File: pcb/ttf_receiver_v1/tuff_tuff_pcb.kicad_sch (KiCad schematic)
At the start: 46 parts, among them J1 Conn_01x02_Socket, J2 Conn_ST_STDC14, J3 TC2070-IDC, J4 Conn_01x02_Pin, J5 Conn_01x04_Pin, Q1 DMG2301L, Q2 DMG3402L, Q3 DMG2301L, Q4 DMG3402L, Q5 DMG2301L, Q6 DMG3402L, Q7 DMG2301L, Q8 DMG3402L, U1 451-00001, U2 TLV76733QWDRBxQ1, U3 MT3608, Y1 Crystal

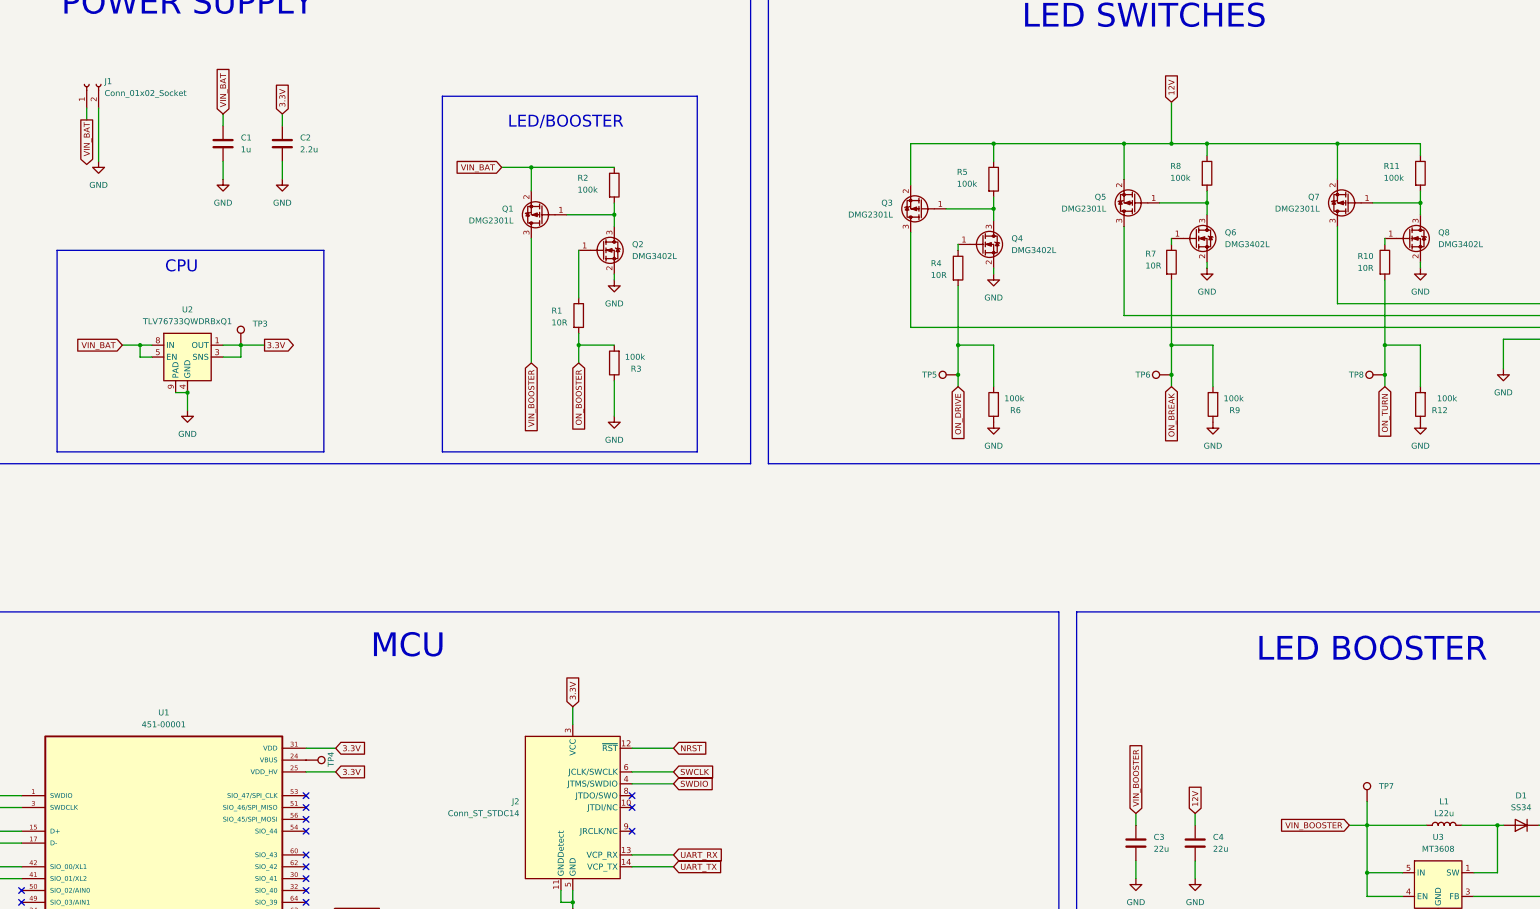
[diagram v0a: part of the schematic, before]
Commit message: feat: Updated ttl schematic
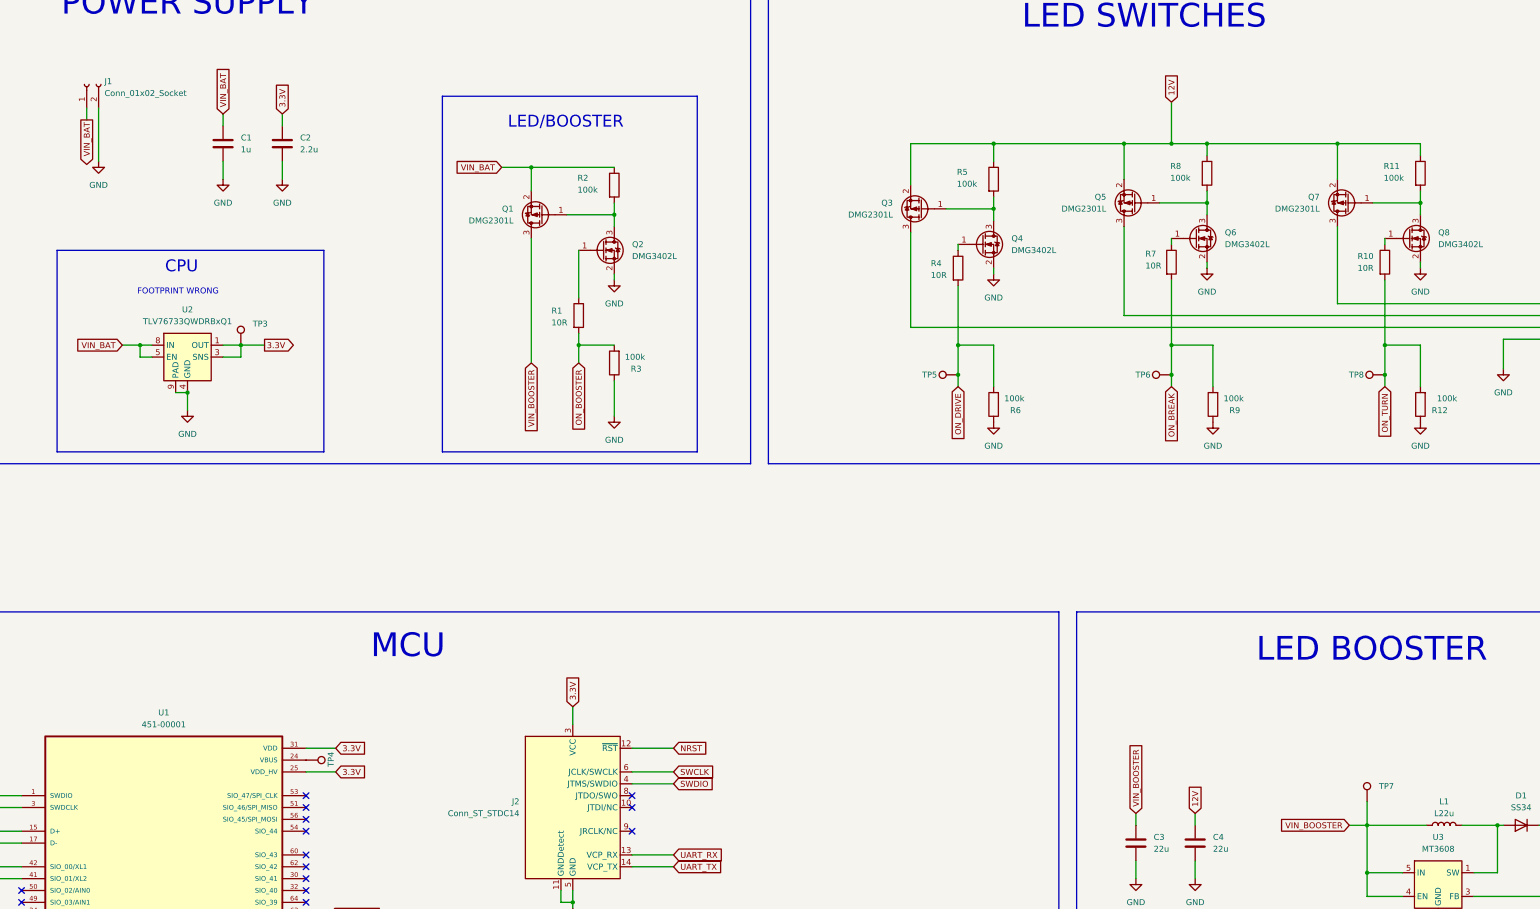
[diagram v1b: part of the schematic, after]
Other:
- note added: "FOOTPRINT WRONG"
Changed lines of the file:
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@@
 (kicad_sch
-	(version 20231120)
+	(version 20250114)
 	(generator "eeschema")
-	(generator_version "8.0")
+	(generator_version "9.0")
 	(paper "A3")
 	(title_block
 		(title "ttl_receiver")
 	)
+	(rectangle
+		(start 44.45 74.93)
+		(end 101.6 118.11)
+		(stroke
+			(width 0)
+			(type default)
+		)
+		(fill
+			(type none)
+		)
+	)
+	(rectangle
+		(start 20.32 16.51)
+		(end 193.04 120.65)
+		(stroke
+			(width 0)
+			(type default)
+		)
+		(fill
+			(type none)
+		)
+	)
+	(rectangle
+		(start 196.85 16.51)
+		(end 398.78 120.65)
+		(stroke
+			(width 0)
+			(type default)
+		)
+		(fill
+			(type none)
+		)
+	)
+	(rectangle
+		(start 127 41.91)
+		(end 181.61 118.11)
+		(stroke
+			(width 0)
+			(type default)
+		)
+		(fill
+			(type none)
+		)
+	)
+	(rectangle
+		(start 15.24 152.4)
+		(end 259.08 283.21)
+		(stroke
+			(width 0)
+			(type default)
+		)
+		(fill
+			(type none)
+		)
+	)
+	(rectangle
+		(start 262.89 152.4)
+		(end 400.05 247.65)
+		(stroke
+			(width 0)
+			(type default)
+		)
+		(fill
+			(type none)
+		)
+	)
+	(text "LED/BOOSTER"
+		(exclude_from_sim no)
+		(at 153.416 47.498 0)
+		(effects
+			(font
+				(size 2.54 2.54)
+			)
+		)
+	)
+	(text "LED BOOSTER"
+		(exclude_from_sim no)
+		(at 326.136 160.528 0)
+		(effects
+			(font
+				(size 5.08 5.08)
+			)
+		)
+	)
+	(text "FOOTPRINT WRONG"
+		(exclude_from_sim no)
+		(at 70.358 83.82 0)
+		(effects
+			(font
+				(size 1.27 1.27)
+			)
+		)
+	)
+	(text "MCU"
+		(exclude_from_sim no)
+		(at 119.634 159.766 0)
+		(effects
+			(font
+				(size 5.08 5.08)
+			)
+		)
+	)
+	(text "CPU"
+		(exclude_from_sim no)
+		(at 71.12 78.486 0)
+		(effects
+			(font
+				(size 2.54 2.54)
+			)
+		)
+	)
+	(text "LED SWITCHES"
+		(exclude_from_sim no)
+		(at 277.368 24.892 0)
+		(effects
+			(font
+				(size 5.08 5.08)
+			)
+		)
+	)
+	(text "POWER SUPPLY"
+		(exclude_from_sim no)
+		(at 72.39 22.098 0)
+		(effects
+			(font
+				(size 5.08 5.08)
+			)
+		)
+	)
 	(junction
 		(at 328.93 95.25)
@@
 		)
 	)
-	(rectangle
-		(start 44.45 74.93)
-		(end 101.6 118.11)
-		(stroke
-			(width 0)
-			(type default)
-		)
-		(fill
-			(type none)
-		)
-	)
-	(rectangle
-		(start 20.32 16.51)
-		(end 193.04 120.65)
-		(stroke
-			(width 0)
-			(type default)
-		)
-		(fill
-			(type none)
-		)
-	)
-	(rectangle
-		(start 196.85 16.51)
-		(end 398.78 120.65)
-		(stroke
-			(width 0)
-			(type default)
-		)
-		(fill
-			(type none)
-		)
-	)
-	(rectangle
-		(start 127 41.91)
-		(end 181.61 118.11)
-		(stroke
-			(width 0)
-			(type default)
-		)
-		(fill
-			(type none)
-		)
-	)
-	(rectangle
-		(start 15.24 152.4)
-		(end 259.08 283.21)
-		(stroke
-			(width 0)
-			(type default)
-		)
-		(fill
-			(type none)
-		)
-	)
-	(rectangle
-		(start 262.89 152.4)
-		(end 400.05 247.65)
-		(stroke
-			(width 0)
-			(type default)
-		)
-		(fill
-			(type none)
-		)
-	)
-	(text "LED/BOOSTER"
-		(exclude_from_sim no)
-		(at 153.416 47.498 0)
-		(effects
-			(font
-				(size 2.54 2.54)
-			)
-		)
-	)
-	(text "LED BOOSTER"
-		(exclude_from_sim no)
-		(at 326.136 160.528 0)
-		(effects
-			(font
-				(size 5.08 5.08)
-			)
-		)
-	)
-	(text "MCU"
-		(exclude_from_sim no)
-		(at 119.634 159.766 0)
-		(effects
-			(font
-				(size 5.08 5.08)
-			)
-		)
-	)
-	(text "CPU"
-		(exclude_from_sim no)
-		(at 71.12 78.486 0)
-		(effects
-			(font
-				(size 2.54 2.54)
-			)
-		)
-	)
-	(text "LED SWITCHES"
-		(exclude_from_sim no)
-		(at 277.368 24.892 0)
-		(effects
-			(font
-				(size 5.08 5.08)
-			)
-		)
-	)
-	(text "POWER SUPPLY"
-		(exclude_from_sim no)
-		(at 72.39 22.098 0)
-		(effects
-			(font
-				(size 5.08 5.08)
-			)
-		)
-	)
 	(global_label "NRST"
 		(shape input)
@@
 		)
 	)
+	(embedded_fonts no)
 )
